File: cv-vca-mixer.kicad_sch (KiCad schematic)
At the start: 46 parts, among them Q901 Q_PNP_BEC, Q902 Q_PNP_BEC, U901 MCP6004, U902 MCP6004, U903 LM13700

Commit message: CV VCA & Mixer, Audio VCA schem capture
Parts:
- C902, C906: footprint (none) -> Capacitor_SMD:C_0603_1608Metric_Pad1.08x0.95mm_HandSolder
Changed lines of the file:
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@@
     (property "Reference" "C906" (id 0) (at 247.65 19.05 90))
     (property "Value" "10p" (id 1) (at 247.65 21.59 90))
-    (property "Footprint" "" (id 2) (at 243.84 27.6352 0)
+    (property "Footprint" "Capacitor_SMD:C_0603_1608Metric_Pad1.08x0.95mm_HandSolder" (id 2) (at 243.84 27.6352 0)
       (effects (font (size 1.27 1.27)) hide)
     )
@@
     (property "Reference" "C902" (id 0) (at 121.92 19.05 90))
     (property "Value" "10p" (id 1) (at 121.92 21.59 90))
-    (property "Footprint" "" (id 2) (at 118.11 27.6352 0)
-      (effects (font (size 1.27 1.27)) hide)
-    )
+    (property "Footprint" "Capacitor_SMD:C_0603_1608Metric_Pad1.08x0.95mm_HandSolder" (id 2) (at 118.11 27.6352 0)
+      (effects (font (size 1.27 1.27)) hide)
+    )

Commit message: CV VCA & Mixer, Audio Mixer layout
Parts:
- renumbered U902 to U901, U901 to U902
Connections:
- net +4.5V: now also U902.10 (+), U902.12 (+), U902.3 (+), U902.5 (+); no longer U902.10 (+), U902.12 (+), U902.3 (+), U902.5 (+)
- net VCA1_Iabc: now also U903.1; no longer U903.16
- net VCA2_Iabc: now also U903.16; no longer U903.1
- net at R905.2, RV902.1: now also U903.3 (+); no longer U903.14 (+)
- net at C903.1, R910.2, R911.2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: now also U902.13 (-); no longer U902.6 (-)
- net at C906.2, R927.1, U901.13 (-): now also U903.12; no longer U903.5
- net at R917.2, RV904.1: now also U903.14 (+); no longer U903.3 (+)
- net at R918.2: now also U903.15 (DIODE_BIAS); no longer U903.2 (DIODE_BIAS)
- net at RV904.3: now also U903.13 (-); no longer U903.4 (-)
- net at C904.1, R919.2, R920.2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: now also U902.2 (-); no longer U902.9 (-)
- net at C904.2, R923.2, R925.1: now also U902.1; no longer U902.8
- net at C905.1, R921.2, R922.2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: now also U902.6 (-); no longer U902.13 (-)
- net at C905.2, R924.2, R926.1: now also U902.7; no longer U902.14
- net at RV902.3: now also U903.4 (-); no longer U903.13 (-)
- net at R907.2: now also U903.2 (DIODE_BIAS); no longer U903.15 (DIODE_BIAS)
- net at C901.1, R902.2, R903.2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: now also U902.9 (-); no longer U902.2 (-)
- net at Q902.1 (B): now also U902.14; no longer U902.7
- net at C902.2, R909.1, U901.6 (-): now also U903.5; no longer U903.12
- net at Q901.1 (B): now also U902.8; no longer U902.1
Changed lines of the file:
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@@
     (pin "6")
   )
-  (symbol (lib_id "Amplifier_Operational:LM13700") (at 215.9 48.26 0) (unit 3)
+  (symbol (lib_id "Amplifier_Operational:LM13700") (at 215.9 48.26 0) (unit 1)
     (in_bom yes) (on_board yes) (fields_autoplaced)
     (property "Reference" "U903" (id 0) (at 215.9 38.1 0))
@@
     (pin "2")
   )
-  (symbol (lib_id "Amplifier_Operational:MCP6004") (at 219.71 157.48 0) (mirror x) (unit 4)
-    (in_bom yes) (on_board yes) (fields_autoplaced)
-    (property "Reference" "U901" (id 0) (at 219.71 147.32 0))
+  (symbol (lib_id "Amplifier_Operational:MCP6004") (at 219.71 157.48 0) (mirror x) (unit 2)
+    (in_bom yes) (on_board yes) (fields_autoplaced)
+    (property "Reference" "U902" (id 0) (at 219.71 147.32 0))
     (property "Value" "MCP6004" (id 1) (at 219.71 149.86 0))
     (property "Footprint" "Package_SO:SOIC-14_3.9x8.7mm_P1.27mm" (id 2) (at 218.44 160.02 0)
@@
     (pin "2")
   )
-  (symbol (lib_id "Amplifier_Operational:MCP6004") (at 134.62 134.62 0) (mirror x) (unit 2)
+  (symbol (lib_id "Amplifier_Operational:MCP6004") (at 134.62 134.62 0) (mirror x) (unit 4)
     (in_bom yes) (on_board yes) (fields_autoplaced)
     (property "Reference" "U902" (id 0) (at 134.62 124.46 0))
@@
     (pin "2")
   )
-  (symbol (lib_id "Amplifier_Operational:LM13700") (at 90.17 48.26 0) (unit 1)
+  (symbol (lib_id "Amplifier_Operational:LM13700") (at 90.17 48.26 0) (unit 3)
     (in_bom yes) (on_board yes) (fields_autoplaced)
     (property "Reference" "U903" (id 0) (at 90.17 38.1 0))
@@
     (pin "2")
   )
-  (symbol (lib_id "Amplifier_Operational:MCP6004") (at 53.34 133.35 0) (mirror x) (unit 1)
+  (symbol (lib_id "Amplifier_Operational:MCP6004") (at 53.34 133.35 0) (mirror x) (unit 3)
     (in_bom yes) (on_board yes) (fields_autoplaced)
     (property "Reference" "U902" (id 0) (at 53.34 123.19 0))
@@
     (pin "2")
   )
-  (symbol (lib_id "Amplifier_Operational:MCP6004") (at 219.71 111.76 0) (mirror x) (unit 3)
+  (symbol (lib_id "Amplifier_Operational:MCP6004") (at 219.71 111.76 0) (mirror x) (unit 1)
     (in_bom yes) (on_board yes) (fields_autoplaced)
     (property "Reference" "U902" (id 0) (at 219.71 101.6 0))
@@
   (symbol (lib_id "Amplifier_Operational:MCP6004") (at 247.65 50.8 0) (mirror x) (unit 4)
     (in_bom yes) (on_board yes) (fields_autoplaced)
-    (property "Reference" "U902" (id 0) (at 247.65 40.64 0))
+    (property "Reference" "U901" (id 0) (at 247.65 40.64 0))
     (property "Value" "MCP6004" (id 1) (at 247.65 43.18 0))
     (property "Footprint" "Package_SO:SOIC-14_3.9x8.7mm_P1.27mm" (id 2) (at 246.38 53.34 0)

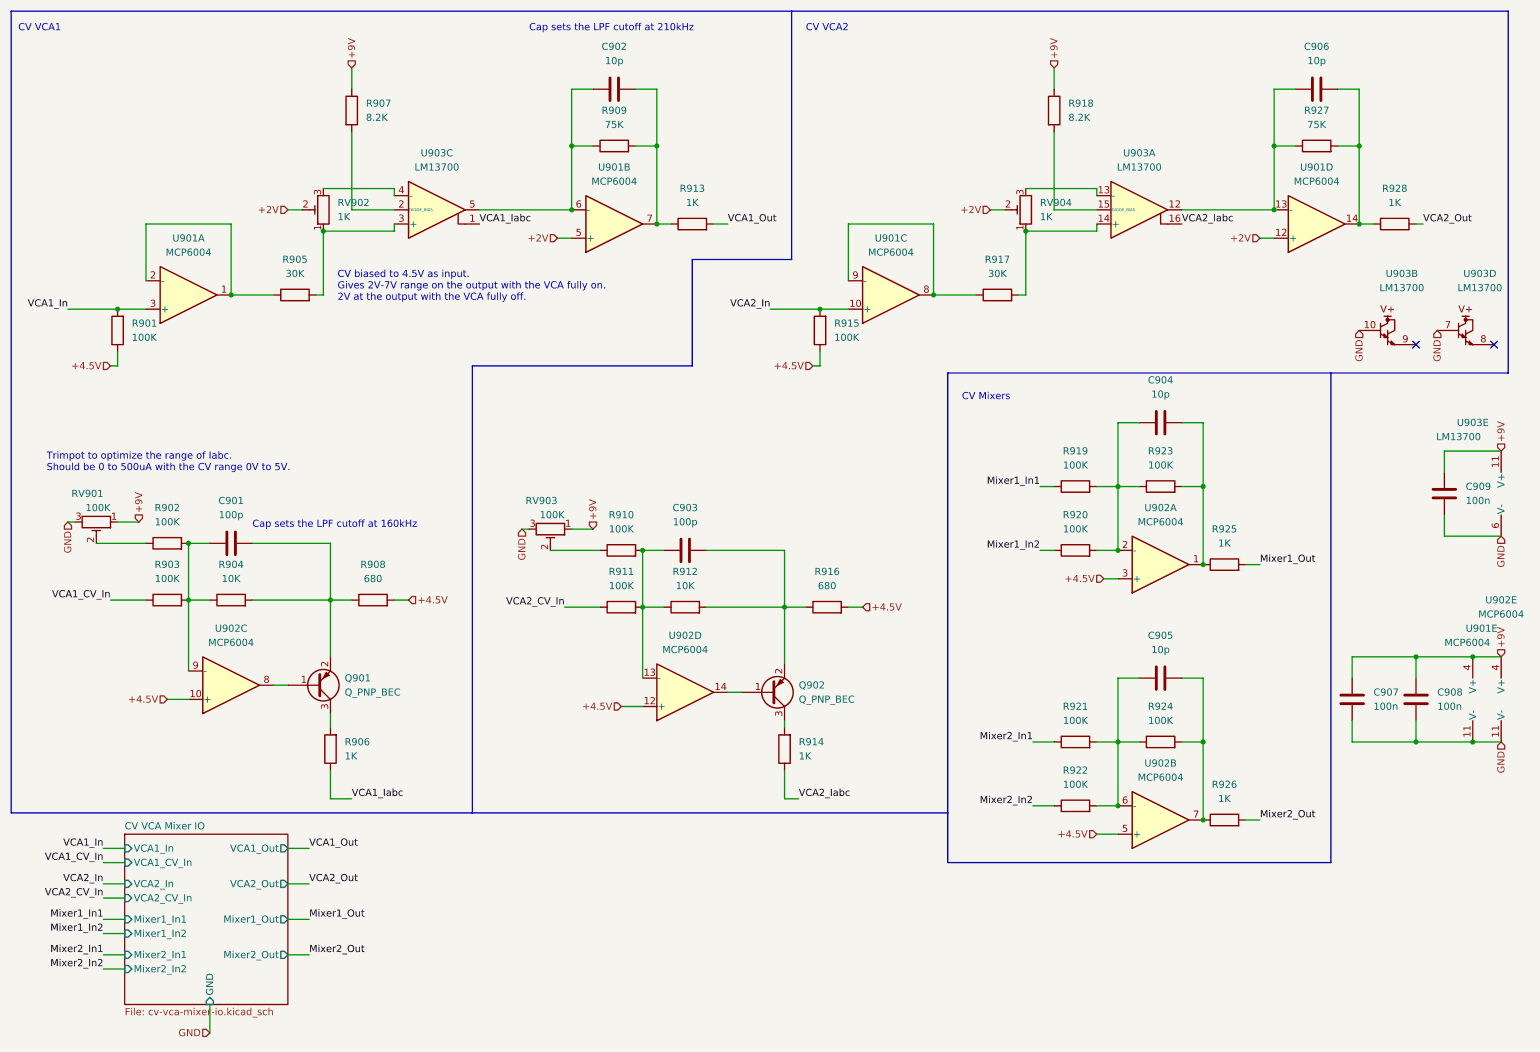
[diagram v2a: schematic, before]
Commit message: LFO schem capture done / replace r2r opamps
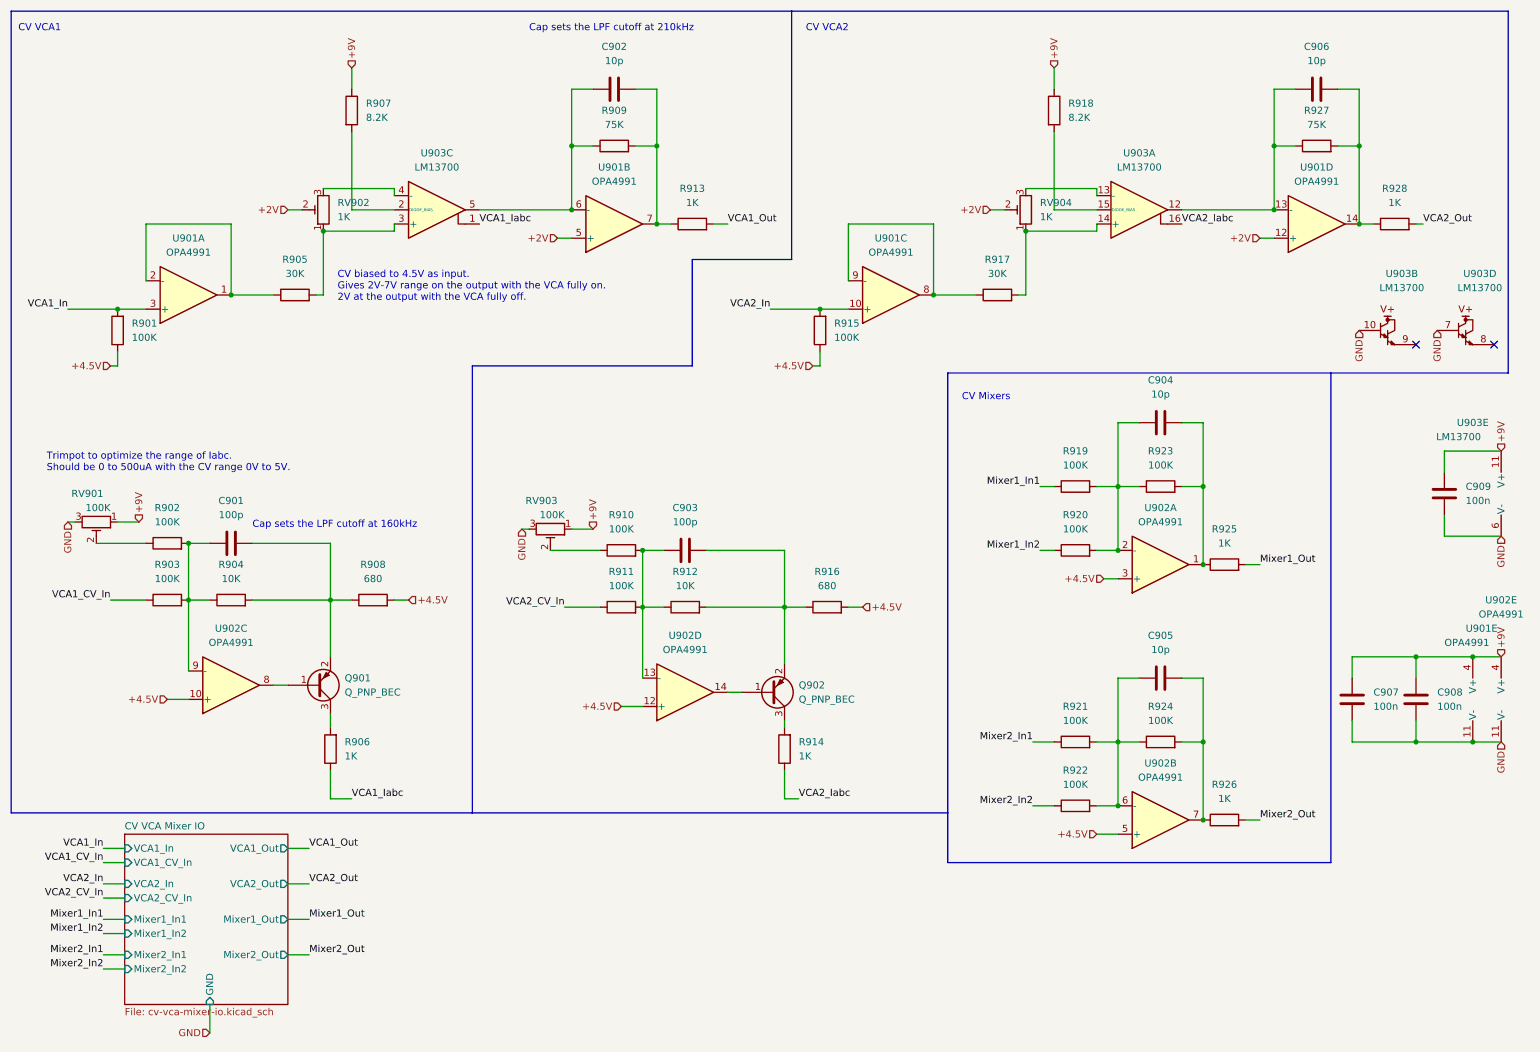
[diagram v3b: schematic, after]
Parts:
- U901, U902: value MCP6004 -> OPA4991
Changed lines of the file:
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@@
     (in_bom yes) (on_board yes) (fields_autoplaced)
     (property "Reference" "U901" (id 0) (at 171.45 53.34 0))
-    (property "Value" "MCP6004" (id 1) (at 171.45 55.88 0))
+    (property "Value" "OPA4991" (id 1) (at 171.45 55.88 0))
     (property "Footprint" "Package_SO:SOIC-14_3.9x8.7mm_P1.27mm" (id 2) (at 170.18 66.04 0)
       (effects (font (size 1.27 1.27)) hide)
@@
     (in_bom yes) (on_board yes) (fields_autoplaced)
     (property "Reference" "U901" (id 0) (at 45.72 53.34 0))
-    (property "Value" "MCP6004" (id 1) (at 45.72 55.88 0))
+    (property "Value" "OPA4991" (id 1) (at 45.72 55.88 0))
     (property "Footprint" "Package_SO:SOIC-14_3.9x8.7mm_P1.27mm" (id 2) (at 44.45 66.04 0)
       (effects (font (size 1.27 1.27)) hide)
@@
       (effects (font (size 1.27 1.27)) (justify left))
     )
-    (property "Value" "MCP6004" (id 1) (at 270.51 125.73 0)
+    (property "Value" "OPA4991" (id 1) (at 270.51 125.73 0)
       (effects (font (size 1.27 1.27)) (justify left))
     )
@@
     (in_bom yes) (on_board yes)
     (property "Reference" "U902" (id 0) (at 280.67 118.11 0))
-    (property "Value" "MCP6004" (id 1) (at 280.67 120.65 0))
+    (property "Value" "OPA4991" (id 1) (at 280.67 120.65 0))
     (property "Footprint" "Package_SO:SOIC-14_3.9x8.7mm_P1.27mm" (id 2) (at 281.94 133.35 0)
       (effects (font (size 1.27 1.27)) hide)
@@
     (in_bom yes) (on_board yes) (fields_autoplaced)
     (property "Reference" "U902" (id 0) (at 219.71 147.32 0))
-    (property "Value" "MCP6004" (id 1) (at 219.71 149.86 0))
+    (property "Value" "OPA4991" (id 1) (at 219.71 149.86 0))
     (property "Footprint" "Package_SO:SOIC-14_3.9x8.7mm_P1.27mm" (id 2) (at 218.44 160.02 0)
       (effects (font (size 1.27 1.27)) hide)
@@
     (in_bom yes) (on_board yes) (fields_autoplaced)
     (property "Reference" "U902" (id 0) (at 134.62 124.46 0))
-    (property "Value" "MCP6004" (id 1) (at 134.62 127 0))
+    (property "Value" "OPA4991" (id 1) (at 134.62 127 0))
     (property "Footprint" "Package_SO:SOIC-14_3.9x8.7mm_P1.27mm" (id 2) (at 133.35 137.16 0)
       (effects (font (size 1.27 1.27)) hide)
@@
     (in_bom yes) (on_board yes) (fields_autoplaced)
     (property "Reference" "U901" (id 0) (at 121.92 40.64 0))
-    (property "Value" "MCP6004" (id 1) (at 121.92 43.18 0))
+    (property "Value" "OPA4991" (id 1) (at 121.92 43.18 0))
     (property "Footprint" "Package_SO:SOIC-14_3.9x8.7mm_P1.27mm" (id 2) (at 120.65 53.34 0)
       (effects (font (size 1.27 1.27)) hide)
@@
     (in_bom yes) (on_board yes) (fields_autoplaced)
     (property "Reference" "U902" (id 0) (at 53.34 123.19 0))
-    (property "Value" "MCP6004" (id 1) (at 53.34 125.73 0))
+    (property "Value" "OPA4991" (id 1) (at 53.34 125.73 0))
     (property "Footprint" "Package_SO:SOIC-14_3.9x8.7mm_P1.27mm" (id 2) (at 52.07 135.89 0)
       (effects (font (size 1.27 1.27)) hide)
@@
     (in_bom yes) (on_board yes) (fields_autoplaced)
     (property "Reference" "U902" (id 0) (at 219.71 101.6 0))
-    (property "Value" "MCP6004" (id 1) (at 219.71 104.14 0))
+    (property "Value" "OPA4991" (id 1) (at 219.71 104.14 0))
     (property "Footprint" "Package_SO:SOIC-14_3.9x8.7mm_P1.27mm" (id 2) (at 218.44 114.3 0)
       (effects (font (size 1.27 1.27)) hide)
@@
     (in_bom yes) (on_board yes) (fields_autoplaced)
     (property "Reference" "U901" (id 0) (at 247.65 40.64 0))
-    (property "Value" "MCP6004" (id 1) (at 247.65 43.18 0))
+    (property "Value" "OPA4991" (id 1) (at 247.65 43.18 0))
     (property "Footprint" "Package_SO:SOIC-14_3.9x8.7mm_P1.27mm" (id 2) (at 246.38 53.34 0)
       (effects (font (size 1.27 1.27)) hide)

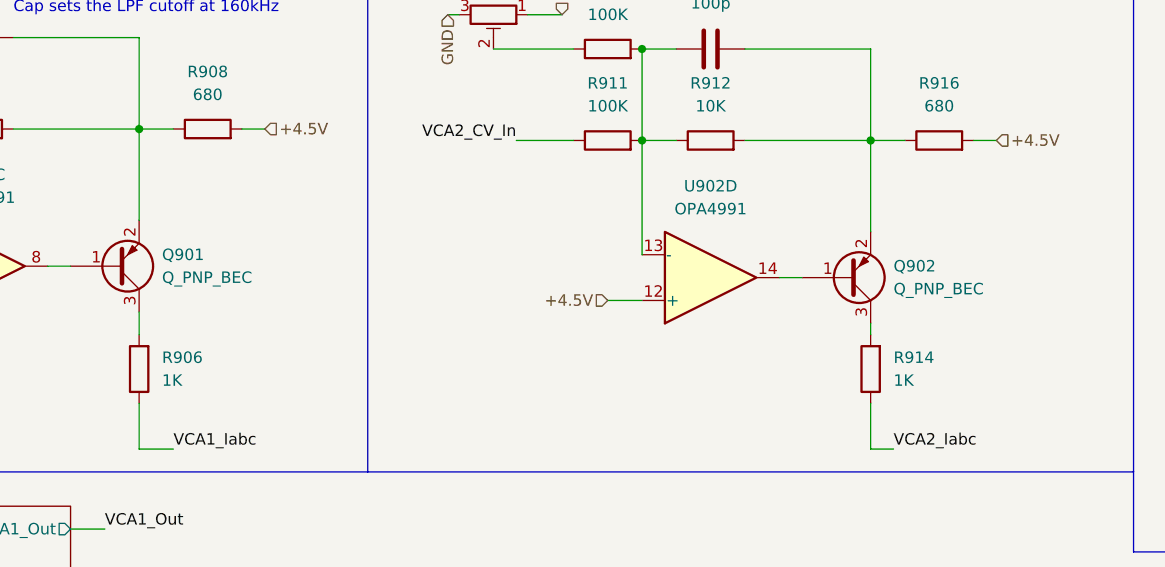
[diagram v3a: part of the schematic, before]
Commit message: Add JLC parts numbers
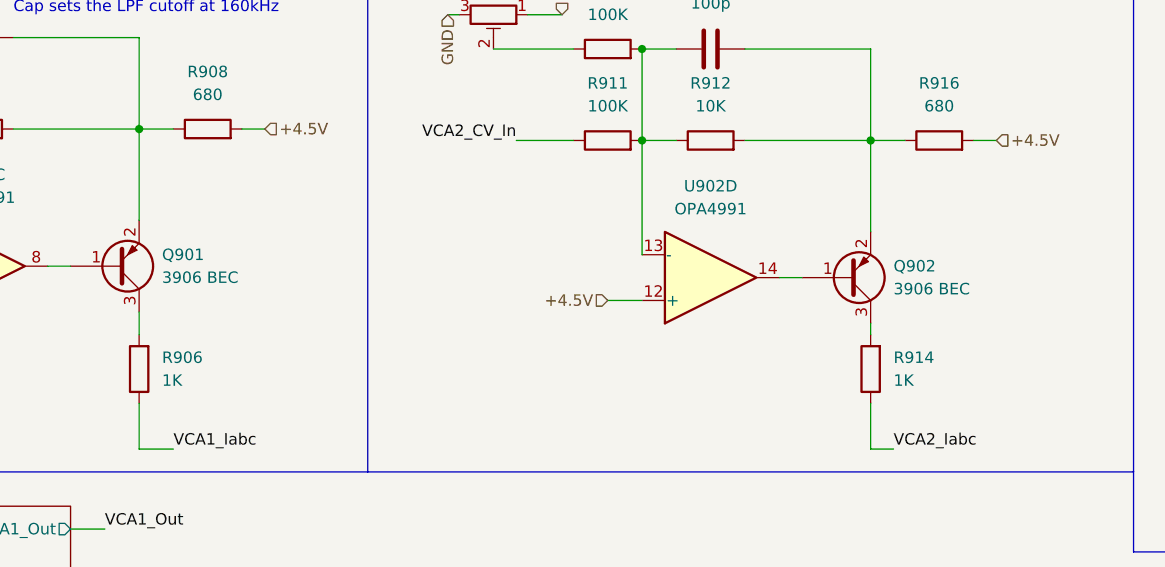
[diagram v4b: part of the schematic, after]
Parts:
- C901, C903: LCSC (none) -> C160903; Role (none) -> opamp-filter
- C902, C904, C905, C906: LCSC (none) -> C91367; Role (none) -> opamp-filter
- C907, C908, C909: LCSC (none) -> C497032; Role (none) -> ic-bypass
- Q901, Q902: value Q_PNP_BEC -> 3906 BEC; LCSC (none) -> C2891809
- R901, R902, R903, R910, R911, R915, R919, R920, R921, R922, R923, R924: LCSC (none) -> C14675
- R904, R912: LCSC (none) -> C98220
- R905, R917: LCSC (none) -> C2907025
- R906, R913, R914, R925, R926, R928: LCSC (none) -> C2907002
- R907, R918: LCSC (none) -> C188034
- R908, R916: LCSC (none) -> C328372
- R909, R927: LCSC (none) -> C101185
- RV901, RV903: LCSC (none) -> C51284
- RV902, RV904: LCSC (none) -> C124615
- U901, U902: LCSC (none) -> C2860973
- U903: LCSC (none) -> C174050
